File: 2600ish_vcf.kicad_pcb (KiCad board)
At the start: 2 copper layers, 50 x 99.8 mm, 95 parts, among them J1 AUDIO IN 1, J2 AUDIO IN 2, J3 OUT, J4 V/OCT IN, J5 CV 1, P1 50K log, P2 50K log, P3 50K lin, P4 100k, P5 50K lin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

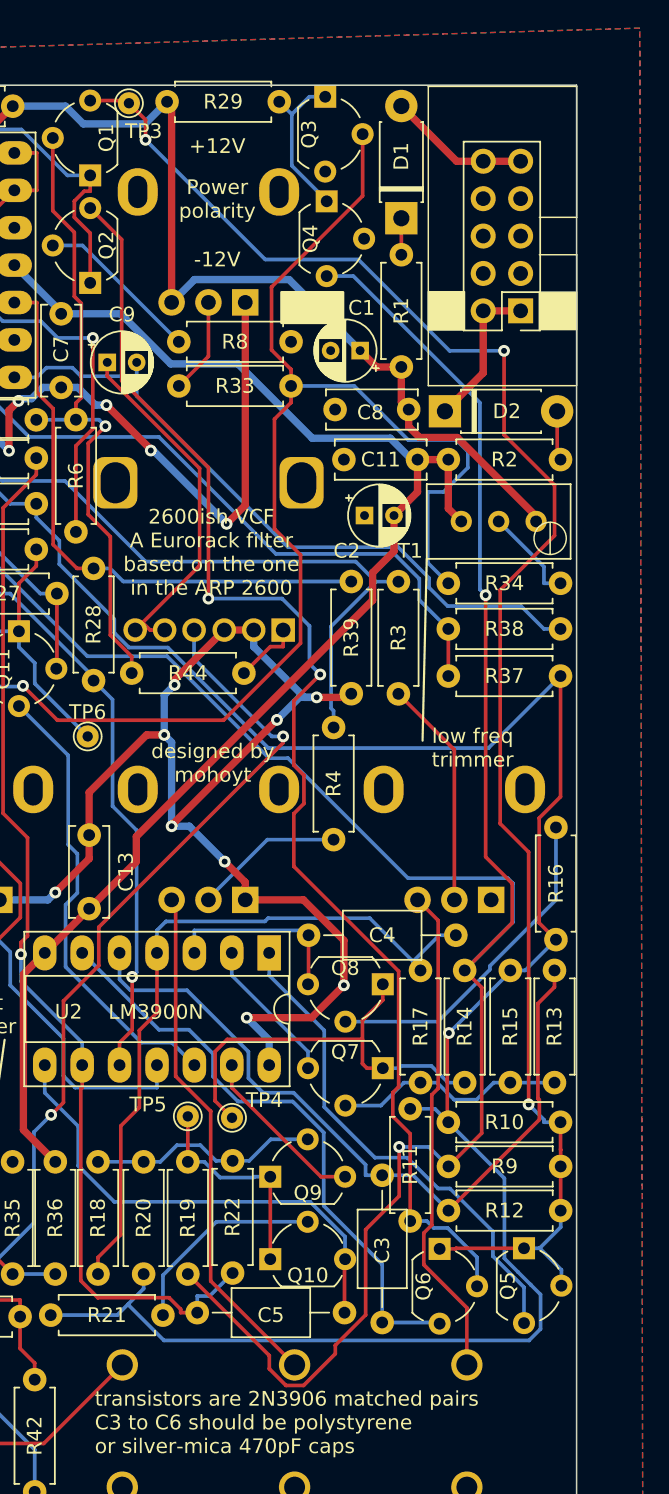
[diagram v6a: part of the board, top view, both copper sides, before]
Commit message: Schematic issue and related routing fixed and v0.2 created. New gerbers generated
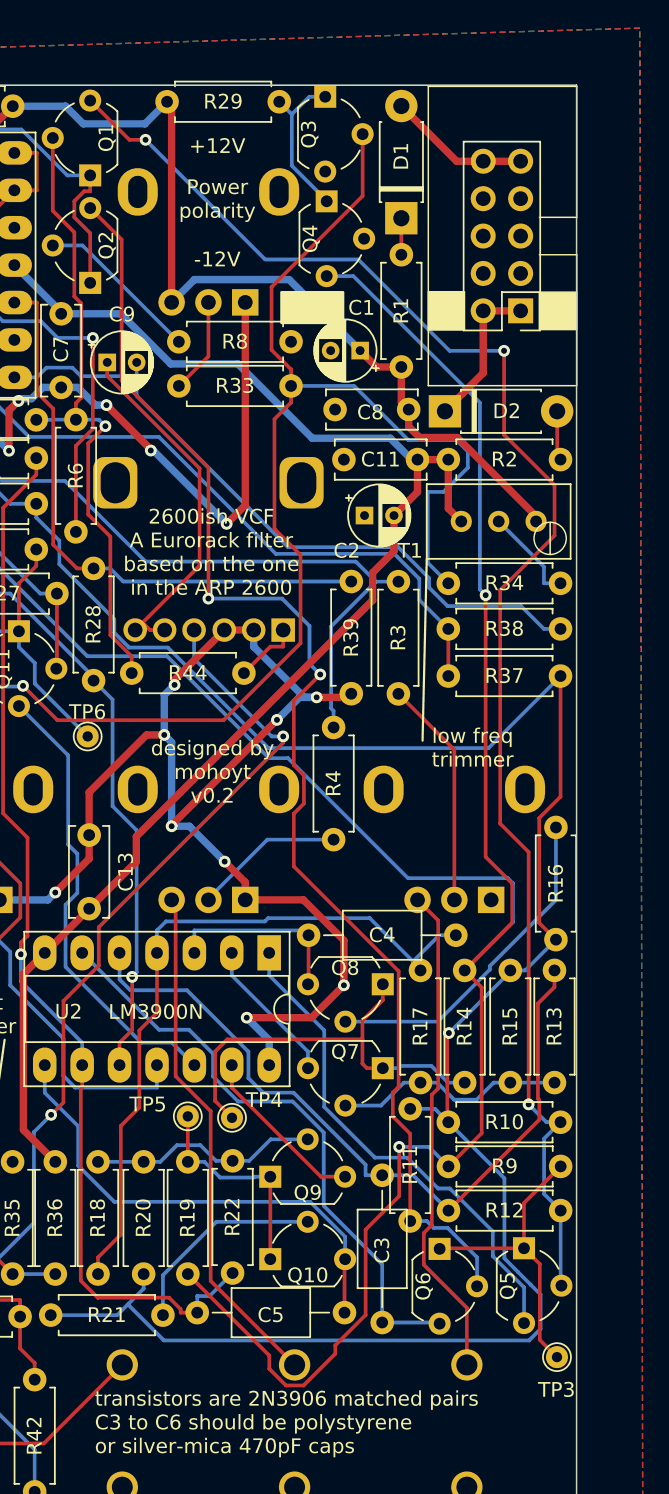
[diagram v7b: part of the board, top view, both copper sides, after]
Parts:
- R35: value 18k -> 10k or 18k
- moved TP3 90.0 mm to (218.0, 144.1)
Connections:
- Q5 pad 1: Net-(Q1-C) -> Net-(Q5-E)
- Q6 pad 1: Net-(Q1-C) -> Net-(Q5-E)
- R9 pad 2: Net-(Q1-C) -> Net-(Q5-E)
- TP3 pad 1: Net-(Q1-C) -> Net-(Q5-E)
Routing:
- net Net-(Q5-E): track 0.00 -> 20.7 mm
- net Net-(Q1-C): track 112.5 -> 104.8 mm
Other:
- board text added: "designed by mohoyt v0.2"
- board text removed: "designed by mohoyt"
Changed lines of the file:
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@@
   (net 60 "AUDIO OUT")
   (net 61 "Net-(R46-Pad1)")
+  (net 62 "Net-(Q5-E)")
   (footprint "Capacitor_THT:C_Disc_D6.0mm_W2.5mm_P5.00mm" (layer "F.Cu")
     (at 203.5 83.1)
@@
   )
   (footprint "TestPoint:TestPoint_THTPad_D1.5mm_Drill0.7mm" (layer "F.Cu")
-    (at 188.9 58.9)
+    (at 217.97 144.05)
     (descr "THT pad as test Point, diameter 1.5mm, hole diameter 0.7mm")
     (tags "test point THT pad")
@@
     (property "ki_keywords" "test point tp")
     (attr exclude_from_pos_files)
-    (fp_text reference "TP3" (at 1 1.9) (layer "F.SilkS")
+    (fp_text reference "TP3" (at -0.02 2.23) (layer "F.SilkS")
         (effects (font (size 1 1) (thickness 0.15)))
     )
@@
       (stroke (width 0.05) (type solid)) (fill none) (layer "F.CrtYd"))
     (pad "1" thru_hole circle (at 0 0) (size 1.5 1.5) (drill 0.7) (layers "*.Cu" "*.Mask")
-      (net 33 "Net-(Q1-C)") (pinfunction "1") (pintype "passive"))
+      (net 62 "Net-(Q5-E)") (pinfunction "1") (pintype "passive"))
   )
   (footprint "Resistor_THT:R_Axial_DIN0207_L6.3mm_D2.5mm_P7.62mm_Horizontal" (layer "F.Cu")
@@
       (stroke (width 0.1) (type solid)) (layer "F.Fab"))
     (pad "1" thru_hole rect (at 0 0 270) (size 1.5 1.5) (drill 0.8) (layers "*.Cu" "*.Mask")
-      (net 33 "Net-(Q1-C)") (pinfunction "E") (pintype "passive"))
+      (net 62 "Net-(Q5-E)") (pinfunction "E") (pintype "passive"))
     (pad "2" thru_hole circle (at 2.54 -2.54 270) (size 1.5 1.5) (drill 0.8) (layers "*.Cu" "*.Mask")
       (net 33 "Net-(Q1-C)") (pinfunction "B") (pintype "input"))
@@
         (effects (font (size 1 1) (thickness 0.15)))
     )
-    (fp_text value "18k" (at 3.81 2.37 90) (layer "F.Fab")
+    (fp_text value "10k or 18k" (at 3.81 2.37 90) (layer "F.Fab")
         (effects (font (size 1 1) (thickness 0.15)))
     )
@@
       (stroke (width 0.1) (type solid)) (layer "F.Fab"))
     (pad "1" thru_hole rect (at 0 0 270) (size 1.5 1.5) (drill 0.8) (layers "*.Cu" "*.Mask")
-      (net 33 "Net-(Q1-C)") (pinfunction "E") (pintype "passive"))
+      (net 62 "Net-(Q5-E)") (pinfunction "E") (pintype "passive"))
     (pad "2" thru_hole circle (at 2.54 -2.54 270) (size 1.5 1.5) (drill 0.8) (layers "*.Cu" "*.Mask")
       (net 35 "Net-(Q2-C)") (pinfunction "B") (pintype "input"))
@@
       (net 38 "Net-(Q4-C)") (pintype "passive"))
     (pad "2" thru_hole oval (at 7.62 0) (size 1.6 1.6) (drill 0.8) (layers "*.Cu" "*.Mask")
-      (net 33 "Net-(Q1-C)") (pintype "passive"))
+      (net 62 "Net-(Q5-E)") (pintype "passive"))
     (model "${KICAD6_3DMODEL_DIR}/Resistor_THT.3dshapes/R_Axial_DIN0207_L6.3mm_D2.5mm_P7.62mm_Horizontal.wrl"
       (offset (xyz 0 0 0))
@@
     (effects (font (size 1 1) (thickness 0.15)) (justify left bottom mirror))
   )
-  (gr_text "designed by \nmohoyt" (at 194.6 105.1) (layer "F.SilkS")
+  (gr_text "designed by \nmohoyt\nv0.2" (at 194.58 106.52) (layer "F.SilkS")
     (effects (font (size 1 1) (thickness 0.15)) (justify bottom))
   )
@@
   (segment (start 190.9432 121.8182) (end 192.9777 121.8182) (width 0.25) (layer "B.Cu") (net 4))
   (segment (start 202.1288 128.7982) (end 202.1288 133.7752) (width 0.25) (layer "B.Cu") (net 4))
-  (segment (start 216.6731 126.49) (end 216.6731 120.0438) (width 0.25) (layer "F.Cu") (net 5))
-  (segment (start 217.8 117.79) (end 217.8 118.9169) (width 0.25) (layer "F.Cu") (net 5))
-  (segment (start 216.7706 127.9294) (end 216.7706 126.5875) (width 0.25) (layer "F.Cu") (net 5))
-  (segment (start 210.6 134.1) (end 216.7706 127.9294) (width 0.25) (layer "F.Cu") (net 5))
+  (segment (start 210.6 134.1) (end 216.7687 127.9313) (width 0.25) (layer "F.Cu") (net 5))
+  (segment (start 216.7687 127.9313) (end 216.7687 126.588295) (width 0.25) (layer "F.Cu") (net 5))
+  (segment (start 216.6731 126.492695) (end 216.6731 120.0438) (width 0.25) (layer "F.Cu") (net 5))
+  (segment (start 217.8 118.9169) (end 217.8 117.79) (width 0.25) (layer "F.Cu") (net 5))
+  (segment (start 216.7687 126.588295) (end 216.6731 126.492695) (width 0.25) (layer "F.Cu") (net 5))
   (segment (start 216.6731 120.0438) (end 217.8 118.9169) (width 0.25) (layer "F.Cu") (net 5))
-  (segment (start 216.7706 126.5875) (end 216.6731 126.49) (width 0.25) (layer "F.Cu") (net 5))
   (segment (start 198.0028 126.0931) (end 200.0807 126.0931) (width 0.25) (layer "B.Cu") (net 5))
   (segment (start 188.265 116.6) (end 188.265 118.4047) (width 0.25) (layer "B.Cu") (net 5))
@@
   (segment (start 182.61 80.4) (end 183.7369 80.4) (width 0.25) (layer "B.Cu") (net 32))
   (segment (start 185.3 80.39) (end 186.8611 80.39) (width 0.25) (layer "B.Cu") (net 32))
-  (segment (start 210 136.7) (end 211.0769 136.7) (width 0.25) (layer "F.Cu") (net 33))
-  (segment (start 186.27 58.72) (end 188.72 58.72) (width 0.25) (layer "F.Cu") (net 33))
+  (segment (start 188.9352 61.3852) (end 190.029 61.3852) (width 0.25) (layer "F.Cu") (net 33))
   (segment (start 216.0437 109.754) (end 214.1108 107.8211) (width 0.25) (layer "F.Cu") (net 33))
-  (segment (start 218.22 129.9731) (end 218.21 129.9631) (width 0.25) (layer "F.Cu") (net 33))
-  (segment (start 218.22 131.1) (end 218.22 129.9731) (width 0.25) (layer "F.Cu") (net 33))
-  (segment (start 218.22 134.1) (end 218.22 131.1) (width 0.25) (layer "F.Cu") (net 33))
   (segment (start 214.1108 107.8211) (end 214.1108 91.9565) (width 0.25) (layer "F.Cu") (net 33))
   (segment (start 217.8014 88.2659) (end 217.8014 84.8364) (width 0.25) (layer "F.Cu") (net 33))
-  (segment (start 218.21 129.9631) (end 218.21 128.1) (width 0.25) (layer "F.Cu") (net 33))
-  (segment (start 215.73 136.66) (end 211.1169 136.66) (width 0.25) (layer "F.Cu") (net 33))
   (segment (start 217.8014 84.8364) (end 214.3746 81.4096) (width 0.25) (layer "F.Cu") (net 33))
-  (segment (start 190.029 60.029) (end 190.029 61.3852) (width 0.25) (layer "F.Cu") (net 33))
-  (segment (start 188.9 58.9) (end 190.029 60.029) (width 0.25) (layer "F.Cu") (net 33))
   (segment (start 214.3746 81.4096) (end 214.3746 75.7125) (width 0.25) (layer "F.Cu") (net 33))
   (segment (start 216.0437 126.8886) (end 216.0437 109.754) (width 0.25) (layer "F.Cu") (net 33))
-  (segment (start 211.1169 136.66) (end 211.0769 136.7) (width 0.25) (layer "F.Cu") (net 33))
+  (segment (start 186.27 58.72) (end 188.9352 61.3852) (width 0.25) (layer "F.Cu") (net 33))
   (segment (start 214.1108 91.9565) (end 217.8014 88.2659) (width 0.25) (layer "F.Cu") (net 33))
   (via (at 216.0437 126.8886) (size 0.8) (drill 0.4) (layers "F.Cu" "B.Cu") (net 33))
   (via (at 190.029 61.3852) (size 0.8) (drill 0.4) (layers "F.Cu" "B.Cu") (net 33))
   (via (at 214.3746 75.7125) (size 0.8) (drill 0.4) (layers "F.Cu" "B.Cu") (net 33))
-  (segment (start 217.0831 128.1) (end 217.0831 127.928) (width 0.25) (layer "B.Cu") (net 33))
   (segment (start 204.4777 69.5113) (end 198.1551 69.5113) (width 0.25) (layer "B.Cu") (net 33))
   (segment (start 198.1551 69.5113) (end 190.029 61.3852) (width 0.25) (layer "B.Cu") (net 33))
-  (segment (start 218.22 135.2269) (end 216.8069 136.64) (width 0.25) (layer "B.Cu") (net 33))
-  (segment (start 215.73 136.66) (end 216.8069 136.66) (width 0.25) (layer "B.Cu") (net 33))
-  (segment (start 217.0831 127.928) (end 216.0437 126.8886) (width 0.25) (layer "B.Cu") (net 33))
-  (segment (start 218.22 134.1) (end 218.22 135.2269) (width 0.25) (layer "B.Cu") (net 33))
-  (segment (start 216.8069 136.64) (end 216.8069 136.66) (width 0.25) (layer "B.Cu") (net 33))
-  (segment (start 218.21 128.1) (end 217.0831 128.1) (width 0.25) (layer "B.Cu") (net 33))
+  (segment (start 217.095 129.215) (end 217.095 132.975) (width 0.25) (layer "B.Cu") (net 33))
+  (segment (start 218.21 128.1) (end 217.2551 128.1) (width 0.25) (layer "B.Cu") (net 33))
+  (segment (start 218.22 139.15) (end 218.27 139.2) (width 0.25) (layer "B.Cu") (net 33))
   (segment (start 214.3746 75.7125) (end 210.6789 75.7125) (width 0.25) (layer "B.Cu") (net 33))
-  (segment (start 216.8069 136.66) (end 218.27 138.1231) (width 0.25) (layer "B.Cu") (net 33))
-  (segment (start 218.27 138.1231) (end 218.27 139.2) (width 0.25) (layer "B.Cu") (net 33))
+  (segment (start 217.095 132.975) (end 218.22 134.1) (width 0.25) (layer "B.Cu") (net 33))
+  (segment (start 218.21 128.1) (end 217.095 129.215) (width 0.25) (layer "B.Cu") (net 33))
+  (segment (start 218.22 134.1) (end 218.22 139.15) (width 0.25) (layer "B.Cu") (net 33))
   (segment (start 210.6789 75.7125) (end 204.4777 69.5113) (width 0.25) (layer "B.Cu") (net 33))
+  (segment (start 217.2551 128.1) (end 216.0437 126.8886) (width 0.25) (layer "B.Cu") (net 33))
   (segment (start 183.73 68.56) (end 185.75 68.56) (width 0.25) (layer "B.Cu") (net 34))
   (segment (start 185.75 68.56) (end 192.29 75.1) (width 0.25) (layer "B.Cu") (net 34))
@@
   (segment (start 170.6 138.99) (end 172.05 137.54) (width 0.25) (layer "F.Cu") (net 61))
   (segment (start 174.59 132) (end 172.05 132) (width 0.25) (layer "B.Cu") (net 61))
+  (segment (start 210.04 136.66) (end 210 136.7) (width 0.25) (layer "F.Cu") (net 62))
+  (segment (start 218.22 131.1) (end 215.73 133.59) (width 0.25) (layer "F.Cu") (net 62))
+  (segment (start 215.73 136.66) (end 216.805 137.735) (width 0.25) (layer "F.Cu") (net 62))
+  (segment (start 215.73 133.59) (end 215.73 136.66) (width 0.25) (layer "F.Cu") (net 62))
+  (segment (start 216.805 137.735) (end 216.805 142.885) (width 0.25) (layer "F.Cu") (net 62))
+  (segment (start 216.805 142.885) (end 217.97 144.05) (width 0.25) (layer "F.Cu") (net 62))
+  (segment (start 215.73 136.66) (end 210.04 136.66) (width 0.25) (layer "F.Cu") (net 62))
   (zone (net 2) (net_name "GND") (layers "F&B.Cu") (hatch edge 0.5)
     (connect_pads (clearance 0.5))
